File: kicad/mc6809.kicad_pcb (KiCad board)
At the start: 2 copper layers, 27 parts, among them U1 TL7705A, U2 MC6809, U3 GAL22V10, U4 74LS138, U5 MC6840_PTM, U6 MC6850_ACIA, U7 MAX202, U8 27C64, U9 628128_DIP32_SSOP32

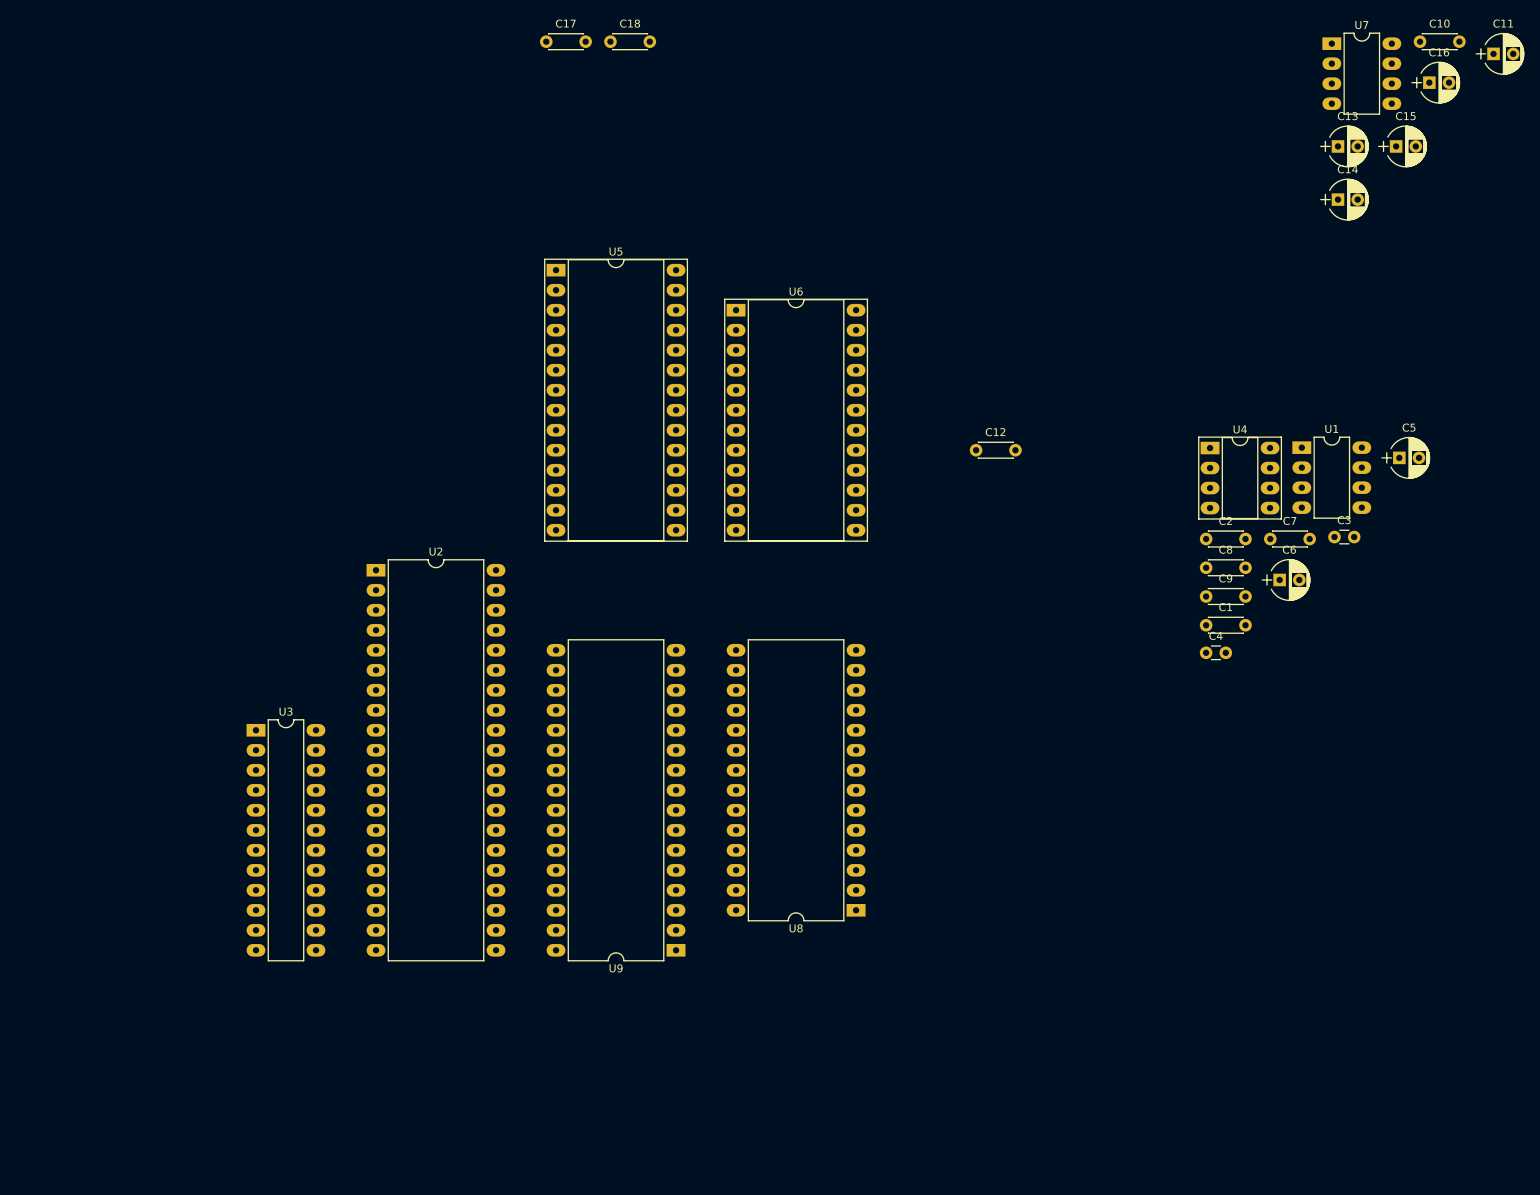
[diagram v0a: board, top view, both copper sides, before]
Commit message: Adding PCB layout
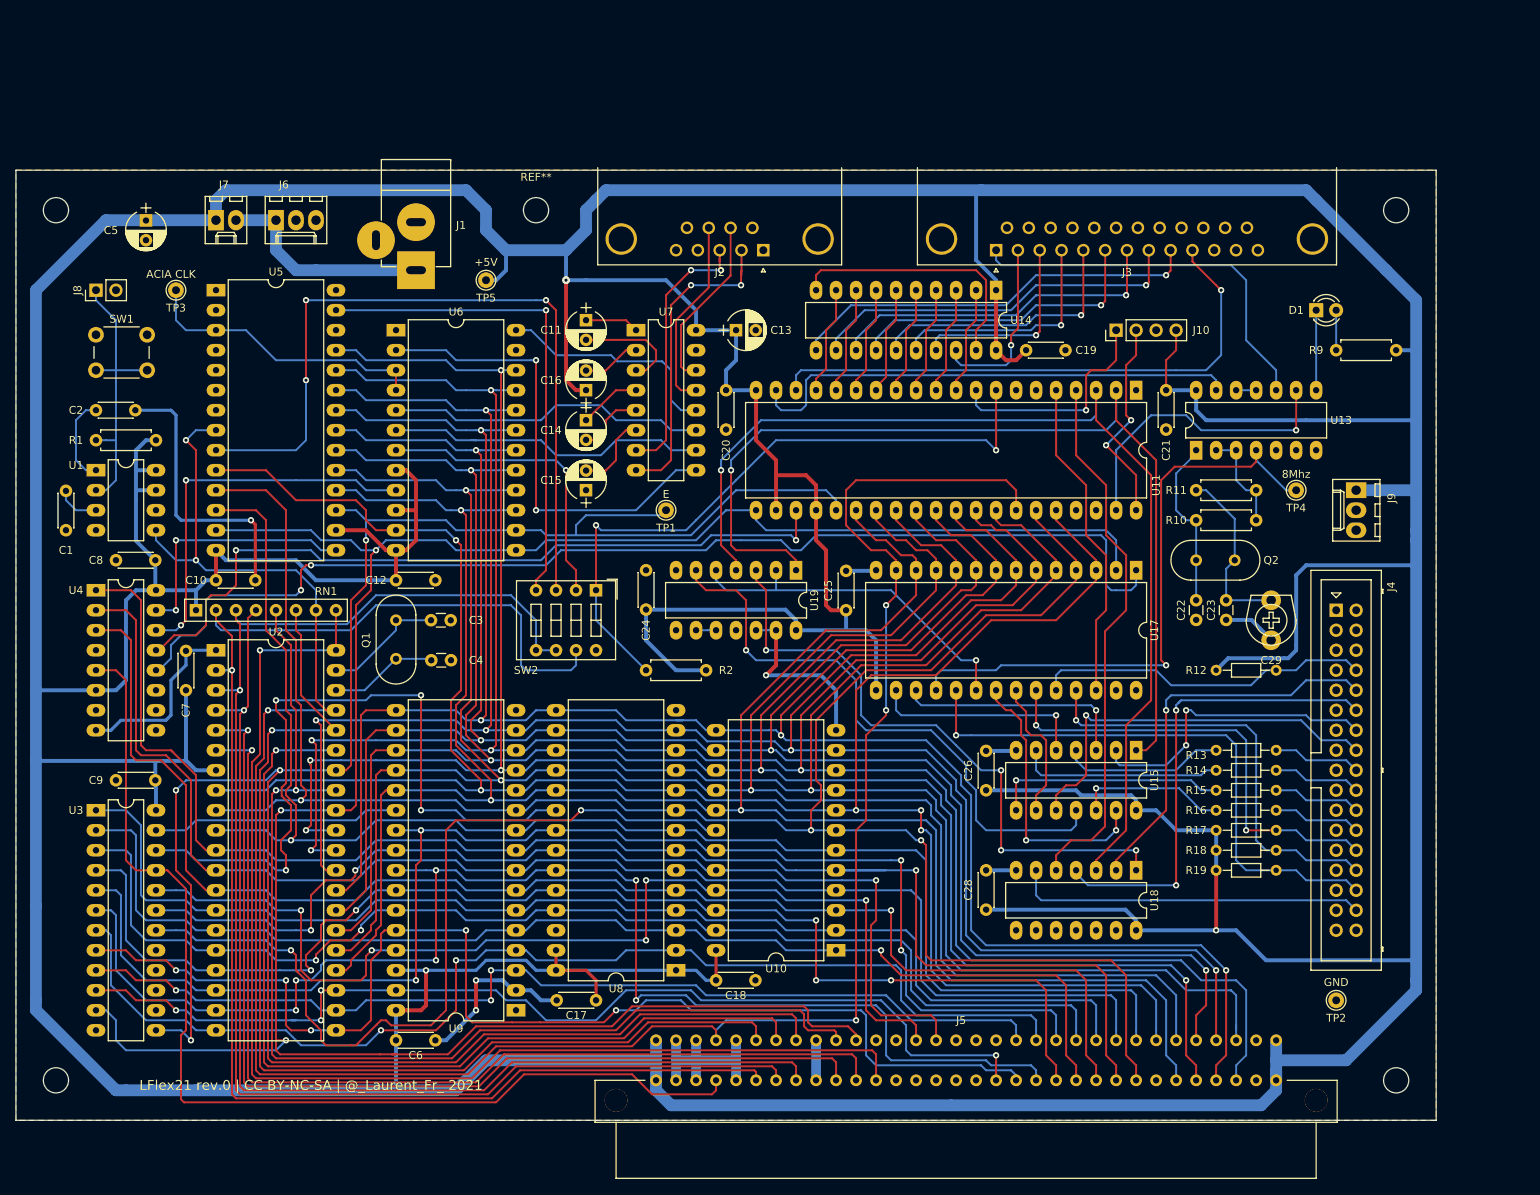
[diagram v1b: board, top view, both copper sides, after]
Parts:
- added C19: 100n, Capacitors_THT:C_Disc_D4.3mm_W1.9mm_P5.00mm, F.Cu at (153.7, 55.9)
- added C20: 100n, Capacitors_THT:C_Disc_D4.3mm_W1.9mm_P5.00mm, F.Cu at (115.6, 61.0)
- added C21: 100n, Capacitors_THT:C_Disc_D4.3mm_W1.9mm_P5.00mm, F.Cu at (171.4, 61.0)
- added C22: 27p, Capacitors_THT:C_Disc_D3.0mm_W1.6mm_P2.50mm, F.Cu at (175.3, 87.6)
- added C23: 22p, Capacitors_THT:C_Disc_D3.0mm_W1.6mm_P2.50mm, F.Cu at (179.1, 87.6)
- added C24: 100n, Capacitors_THT:C_Disc_D4.3mm_W1.9mm_P5.00mm, F.Cu at (105.4, 88.8)
- added C25: 100n, Capacitors_THT:C_Disc_D4.3mm_W1.9mm_P5.00mm, F.Cu at (130.8, 88.9)
- added C26: 100n, Capacitors_THT:C_Disc_D4.3mm_W1.9mm_P5.00mm, F.Cu at (148.6, 111.8)
- added C28: 100n, Capacitors_THT:C_Disc_D4.3mm_W1.9mm_P5.00mm, F.Cu at (148.6, 126.9)
- added C29: 5-15pF, mylib:C-TRIMMER-5, F.Cu at (184.8, 90.2)
- added D1: LED, LEDs:LED_D3.0mm, F.Cu at (190.5, 50.8)
- added J1: Conn_01x02_Male, Connectors:JACK_ALIM, F.Cu at (76.2, 45.7)
- added J10: Conn_01x04_Male, Pin_Headers:Pin_Header_Straight_1x04_Pitch2.54mm, F.Cu at (165.1, 53.3)
- added J2: DB9_Male, Connectors_DSub:DSUB-9_Male_Horizontal_Pitch2.77x2.84mm_EdgePinOffset7.70mm_Housed_MountingHolesOffset9.12mm, F.Cu at (120.3, 43.2)
- added J3: DB25_Female, Connectors_DSub:DSUB-25_Female_Horizontal_Pitch2.77x2.84mm_EdgePinOffset7.70mm_Housed_MountingHolesOffset9.12mm, F.Cu at (149.9, 43.2)
- added J4: Conn_02x17_Odd_Even, Connectors_Multicomp:Multicomp_MC9A12-3434_2x17x2.54mm_Straight, F.Cu at (193.0, 88.9)
- added J5: DIN41612-a+c, mylib:Socket_DIN41612-CaseC1-AC-Male-64Pin-2rows, F.Cu at (146.1, 146.1)
- added J6: Conn_01x03_Male, Connectors_Molex:Molex_KK-6410-03_03x2.54mm_Straight, F.Cu at (58.4, 39.4)
- added J7: Conn_01x02_Male, Connectors_Molex:Molex_KK-6410-02_02x2.54mm_Straight, F.Cu at (50.8, 39.4)
- added J8: Conn_01x02_Male, Pin_Headers:Pin_Header_Straight_1x02_Pitch2.54mm, F.Cu at (35.6, 48.3)
- added J9: Conn_01x03_Male, Connectors_Molex:Molex_KK-6410-03_03x2.54mm_Straight, F.Cu at (195.6, 73.7)
- added Q1: 3.6864Mhz, Crystals:Crystal_HC18-U_Vertical, F.Cu at (73.7, 90.2)
- added Q2: 8Mhz, Crystals:Crystal_HC18-U_Vertical, F.Cu at (175.3, 82.5)
- added R1: 10k, Resistors_THT:R_Axial_DIN0207_L6.3mm_D2.5mm_P7.62mm_Horizontal, F.Cu at (35.6, 67.3)
- added R10: 4.7M, Resistors_THT:R_Axial_DIN0207_L6.3mm_D2.5mm_P7.62mm_Horizontal, F.Cu at (182.9, 77.5)
- added R11: 1k, Resistors_THT:R_Axial_DIN0207_L6.3mm_D2.5mm_P7.62mm_Horizontal, F.Cu at (175.3, 73.7)
- added R12: 1K, Resistors_THT:R_Axial_DIN0204_L3.6mm_D1.6mm_P7.62mm_Horizontal, F.Cu at (185.4, 96.5)
- added R13: 47, Resistors_THT:R_Axial_DIN0204_L3.6mm_D1.6mm_P7.62mm_Horizontal, F.Cu at (177.8, 106.7)
- added R14: 47, Resistors_THT:R_Axial_DIN0204_L3.6mm_D1.6mm_P7.62mm_Horizontal, F.Cu at (177.8, 109.2)
- added R15: 47, Resistors_THT:R_Axial_DIN0204_L3.6mm_D1.6mm_P7.62mm_Horizontal, F.Cu at (177.8, 111.8)
- added R16: 47, Resistors_THT:R_Axial_DIN0204_L3.6mm_D1.6mm_P7.62mm_Horizontal, F.Cu at (177.8, 114.3)
- added R17: 1K, Resistors_THT:R_Axial_DIN0204_L3.6mm_D1.6mm_P7.62mm_Horizontal, F.Cu at (177.8, 116.8)
- added R18: 1K, Resistors_THT:R_Axial_DIN0204_L3.6mm_D1.6mm_P7.62mm_Horizontal, F.Cu at (177.8, 119.4)
- added R19: 220, Resistors_THT:R_Axial_DIN0204_L3.6mm_D1.6mm_P7.62mm_Horizontal, F.Cu at (177.8, 121.9)
- added R2: 4k7, Resistors_THT:R_Axial_DIN0207_L6.3mm_D2.5mm_P7.62mm_Horizontal, F.Cu at (113.0, 96.5)
- added R9: 1k, Resistors_THT:R_Axial_DIN0207_L6.3mm_D2.5mm_P7.62mm_Horizontal, F.Cu at (200.7, 55.9)
- added REF**: MountingHole_3.2mm_M3, Mounting_Holes:MountingHole_3.2mm_M3, F.Cu at (91.4, 38.1)
- added REF**: MountingHole_3.2mm_M3, Mounting_Holes:MountingHole_3.2mm_M3, F.Cu at (200.7, 38.1)
- added REF**: MountingHole_3.2mm_M3, Mounting_Holes:MountingHole_3.2mm_M3, F.Cu at (200.7, 148.6)
- added REF**: MountingHole_3.2mm_M3, Mounting_Holes:MountingHole_3.2mm_M3, F.Cu at (30.5, 148.6)
- added REF**: MountingHole_3.2mm_M3, Mounting_Holes:MountingHole_3.2mm_M3, F.Cu at (30.5, 38.1)
- added RN1: 4k7, Resistors_THT:R_Array_SIP8, F.Cu at (48.3, 88.9)
- added SW1: SW_Push, Buttons_Switches_THT:SW_PUSH_6mm, F.Cu at (35.6, 53.9)
- added SW2: SW_DIP_x04, Buttons_Switches_THT:SW_DIP_x4_W7.62mm_Slide, F.Cu at (99.1, 86.4)
- added TP1: E, Connectors:Pin_d1.0mm_L10.0mm, F.Cu at (108.0, 76.2)
- added TP2: GND, Connectors:Pin_d1.0mm_L10.0mm, F.Cu at (193.0, 138.4)
- added TP3: Acia_Clk, Connectors:Pin_d1.0mm_L10.0mm, F.Cu at (45.7, 48.3)
- added TP4: Floppy_8mhz, Connectors:Pin_d1.0mm_L10.0mm, F.Cu at (188.0, 73.7)
- added TP5: +5V, Connectors:Pin_d1.0mm_L10.0mm, F.Cu at (85.1, 47.0)
- added U10: MK48T12, Housings_DIP:DIP-24_W15.24mm_LongPads, F.Cu at (129.5, 132.1)
- added U11: 6821, Housings_DIP:DIP-40_W15.24mm_LongPads, F.Cu at (167.6, 61.0)
- added U13: 74HC04, Housings_DIP:DIP-14_W7.62mm_LongPads, F.Cu at (175.3, 68.6)
- added U14: 74LS245, Housings_DIP:DIP-20_W7.62mm_LongPads, F.Cu at (149.9, 48.3)
- added U15: 74LS06, Housings_DIP:DIP-14_W7.62mm_LongPads, F.Cu at (167.6, 106.7)
- added U17: WD1770, Housings_DIP:DIP-28_W15.24mm_LongPads, F.Cu at (167.6, 83.8)
- added U18: 74LS06, Housings_DIP:DIP-14_W7.62mm_LongPads, F.Cu at (167.6, 121.9)
- added U19: 74LS08, Housings_DIP:DIP-14_W7.62mm_LongPads, F.Cu at (124.5, 83.8)
- C1: value 100n -> 220n
- C5: value 33u -> 47u/16V
- C6: value 33u -> 100n; footprint Capacitors_THT:CP_Radial_D5.0mm_P2.50mm -> Capacitors_THT:C_Disc_D4.3mm_W1.9mm_P5.00mm
- U4: footprint Housings_DIP:DIP-8_W7.62mm_Socket_LongPads -> Housings_DIP:DIP-16_W7.62mm_LongPads
- U5: footprint Housings_DIP:DIP-28_W15.24mm_Socket_LongPads -> Housings_DIP:DIP-28_W15.24mm_LongPads
- U6: footprint Housings_DIP:DIP-24_W15.24mm_Socket_LongPads -> Housings_DIP:DIP-24_W15.24mm_LongPads
- U7: footprint Housings_DIP:DIP-8_W7.62mm_LongPads -> Housings_DIP:DIP-16_W7.62mm_LongPads
- moved C10 167.5 mm to (50.8, 85.1)
- moved C5 162.0 mm to (41.9, 39.4), turned to 270 degrees
- moved U1 153.1 mm to (35.6, 71.1)
- moved C1 145.8 mm to (31.8, 73.7), turned to 270 degrees
- moved U4 142.6 mm to (35.6, 86.4)
- moved C2 141.9 mm to (35.6, 63.5)
- moved C7 139.0 mm to (47.0, 99.1), turned to 90 degrees
- moved C9 135.5 mm to (43.1, 110.5), turned to 180 degrees
- moved C8 133.4 mm to (43.1, 82.5), turned to 180 degrees
- moved C6 126.5 mm to (73.7, 143.5)
- moved C17 121.9 mm to (99.1, 138.4), turned to 180 degrees
- moved C11 120.1 mm to (97.8, 52.1), turned to 270 degrees
- moved C18 119.9 mm to (114.3, 135.9)
- moved C3 115.2 mm to (78.1, 90.2)
- moved C16 114.0 mm to (97.8, 61.0), turned to 90 degrees
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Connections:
- net /cpu6809/~CSIO~ renamed ~CSIO~
- U1 pad 5: /cpu6809/~RESET~ -> ~RESET~
- U2 pad 2: /cpu6809/~NMI~ -> ~NMI~
- U2 pad 3: /cpu6809/~IRQ~ -> ~IRQ~
- U2 pad 32: /cpu6809/R~W~ -> R~W~
- U2 pad 33: Net-(R7-Pad1) -> ~DMA~
- U2 pad 34: Net-(U2-Pad34) -> E
- U2 pad 35: Net-(U2-Pad35) -> Q
- U2 pad 36: Net-(U2-Pad36) -> ~MRDY~
- U2 pad 37: /cpu6809/~RESET~ -> ~RESET~
- U2 pad 4: /cpu6809/~FIRQ~ -> ~FIRQ~
- U2 pad 40: Net-(R5-Pad1) -> ~HALT~
- U2 pad 5: Net-(U2-Pad5) -> BS
- U2 pad 6: Net-(U2-Pad6) -> BA
- U3 pad 11: /cpu6809/R~W~ -> R~W~
- U3 pad 13: Net-(U2-Pad34) -> E
- U3 pad 18: Net-(U3-Pad18) -> ~CSRTC~
- U3 pad 22: /cpu6809/~CSROM~ -> ~CSROM~
- U3 pad 23: /cpu6809/~CSRAM~ -> ~CSRAM~
- U5 pad 13: /serial/R~W~ -> R~W~
- U5 pad 15: /serial/~CSPTM~ -> ~CSPTM~
- U5 pad 17: /serial/E -> E
- U5 pad 8: /serial/~RESET~ -> ~RESET~
- U6 pad 13: /serial/R~W~ -> R~W~
- U6 pad 14: /serial/E -> E
- U6 pad 9: /serial/~CSACIA~ -> ~CSACIA~
- U8 pad 20: /mem/~CSROM~ -> ~CSROM~
- U8 pad 22: /mem/~RD~ -> ~RD~
- U9 pad 22: /mem/~CSRAM~ -> ~CSRAM~
- U9 pad 24: /mem/~RD~ -> ~RD~
- U9 pad 29: /mem/~WR~ -> ~WR~
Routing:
- net +5V: track 0.00 -> 1190.0 mm, vias 0 -> 3
- net R~W~: track 0.00 -> 308.2 mm, vias 0 -> 3
- net D1: track 0.00 -> 301.1 mm, vias 0 -> 5
- net ~RESET~: track 0.00 -> 296.9 mm, vias 0 -> 6
- net D0: track 0.00 -> 296.7 mm, vias 0 -> 5
- net D2: track 0.00 -> 289.5 mm, vias 0 -> 5
- net D3: track 0.00 -> 287.2 mm, vias 0 -> 4
- net E: track 0.00 -> 285.4 mm, vias 0 -> 4
- net D5: track 0.00 -> 281.7 mm, vias 0 -> 4
- net A0: track 0.00 -> 280.8 mm, vias 0 -> 5
- net D4: track 0.00 -> 278.6 mm, vias 0 -> 4
- net D7: track 0.00 -> 277.6 mm, vias 0 -> 3
- net D6: track 0.00 -> 274.8 mm, vias 0 -> 3
- net A1: track 0.00 -> 262.6 mm, vias 0 -> 3
- net A3: track 0.00 -> 193.8 mm, vias 0 -> 1
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- added copper zone on F.Cu, net GND
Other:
- board outline added: 180.3 x 120.6 mm
- board text added: "+5V"
- board text added: "8Mhz"
- board text added: "ACIA CLK"
- board text added: "E"
- board text added: "GND"
- board text added: "LFlex21 rev.0 | CC BY-NC-SA | @_Laurent_Fr_ 2021"

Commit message: Adding PCB
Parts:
- J10: value Conn_01x04_Male -> Conn_01x06_Male; footprint Pin_Headers:Pin_Header_Straight_1x04_Pitch2.54mm -> Pin_Headers:Pin_Header_Straight_1x06_Pitch2.54mm
- J5: footprint mylib:Socket_DIN41612-CaseC1-AC-Male-64Pin-2rows -> mylib:Socket_DIN41612-CaseC1-AC-Male-64Pin-2rows-nosilk
- moved J10 10.8 mm to (175.9, 52.7), turned to 270 degrees
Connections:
- J10 pad 1: Net-(J10-Pad1) -> +5V
- J10 pad 2: Net-(J10-Pad2) -> GND
- J10 pad 3: GND -> Net-(J10-Pad3)
- J10 pad 4: +5V -> Net-(J10-Pad4)
- U11 pad 40: Net-(J10-Pad2) -> Net-(J10-Pad3)
- U11 pad 6: Net-(U11-Pad6) -> Net-(J10-Pad5)
- U11 pad 7: Net-(U11-Pad7) -> Net-(J10-Pad6)
- U11 pad 9: Net-(J10-Pad1) -> Net-(J10-Pad4)
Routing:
- net Net-(J10-Pad4): track 0.00 -> 31.7 mm, vias 0 -> 1
- net Net-(J10-Pad1): track 29.0 -> 0.00 mm, vias 1 -> 0
- net Net-(J10-Pad3): track 0.00 -> 28.5 mm, vias 0 -> 2
- net Net-(J10-Pad2): track 26.5 -> 0.00 mm, vias 2 -> 0
- net Net-(J10-Pad6): track 0.00 -> 17.6 mm
- net GND: track 187.1 -> 204.6 mm
- net Net-(J10-Pad5): track 0.00 -> 17.3 mm
- net +5V: track 1190.0 -> 1191.2 mm
- net /serial/RxD: track 39.6 -> 39.1 mm
